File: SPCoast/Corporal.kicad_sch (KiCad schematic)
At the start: 36 parts, among them SW11829 829, SW11831 831, SW11900 829D, SW11901 1

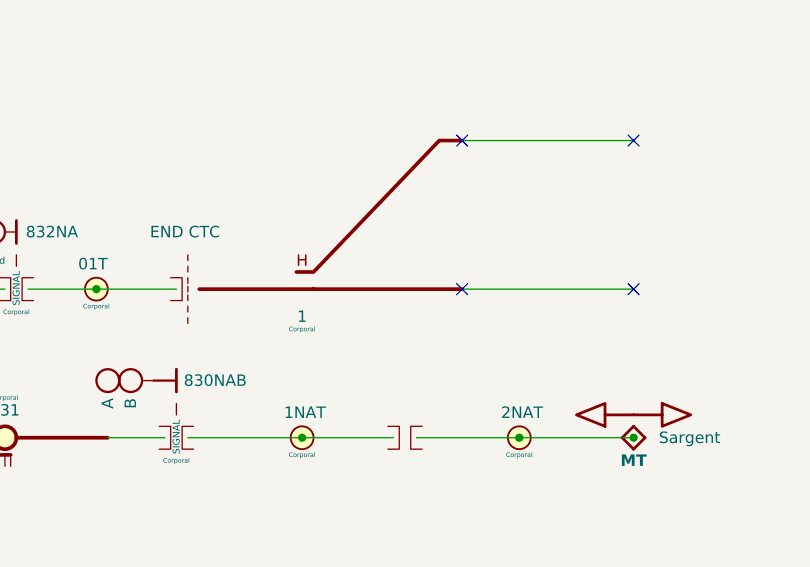
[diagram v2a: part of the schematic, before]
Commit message: feat(spcoast): every sheet on the four Railroad libraries (checkpoint step 6, mechanical half)
By SPCoast/edits/2026-10-12-migrate-libraries.py, run once with KiCad closed: 483 instances
remapped across 16 sheets, embedded definitions replaced by the library blocks, instance fields
synced (Kind, ControlToken, Vital, NormalIs, Chain, Index dropped; Indications renamed
IndicationCeiling; Hold_ms renamed hold_ms; a pixel's Index became its Address; Rulebook kept
on the four Luchessa markers because the compiler still reads it), and 22 units added at the
same position for the plates and devices that are multi-unit now. Owner's choices: every plant
head CPL; Sargent's semaphore UQ; the 0x27 PCA9685 as PWM; the office MAX7313s as the
SPCoastcTc variant. Left by hand: the two AUXILIARY_TRAFFIC markers on Watsonville (retired).

Verified (production/migration-gate.txt, netlist_diff.py against pre-migration.net): office
and local plates and all chips keep their connectivity; 14 nets lost, all on Sargent, where
the six field devices (DevSW13001, 13004 to 13007, 13012) have new pin positions and must be
re-wired by hand. ERC: lib_symbol_issues 492 before (unregistered libraries) to 2 after (the
retired markers); the 29 unconnected pins are those devices and their chip pins.

Co-Authored-By: Claude Fable 5.1 <noreply@anthropic.com>
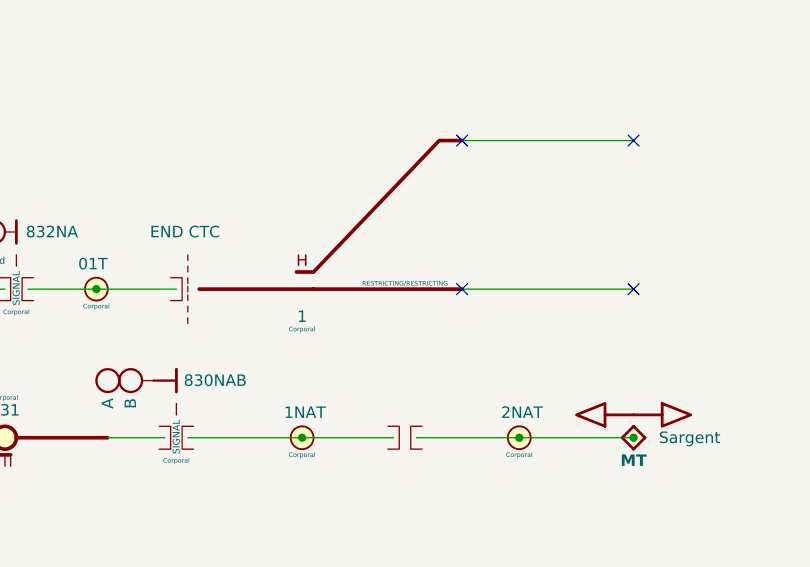
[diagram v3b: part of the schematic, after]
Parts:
- B11001, B11002, B11004, B11005: symbol Railroad:IRJ-Signal -> Railroad-Trackplan:IRJ-Signal
- B11003: symbol Railroad:IRJ-END_CTC -> Railroad-Trackplan:IRJ-END_CTC
- B11006, B11007: symbol Railroad:IRJ -> Railroad-Trackplan:IRJ
- CP11001, CP11002, CP11003: symbol Railroad:NextCP -> Railroad-Trackplan:NextCP
- DOT11002: symbol Railroad:Rule251-DoT-Left -> Railroad-Trackplan:Rule251-DoT-Left
- DOT11003: symbol Railroad:Rule251-DoT-Right -> Railroad-Trackplan:Rule251-DoT-Right
- DOT11004: symbol Railroad:Rule261-DoT-BiDirectional -> Railroad-Trackplan:Rule261-DoT-BiDirectional
- DOT11006: symbol Railroad:Rule105-RestrictedSpeed -> Railroad-Trackplan:Rule105-RestrictedSpeed
- H11001, H11002, H11003, H11004, H11005, H11006: symbol Railroad:Signal Head - CL -> Railroad-Trackplan:Signal Head - CPL; Appliance (none) -> head; Kind HEAD -> (none); Style (none) -> CPL
- HOUSE11001: symbol Railroad:MAIN HOUSE -> Railroad-Trackplan:MAIN HOUSE
- MC11001: symbol Railroad:MaintainerCall -> Railroad-Trackplan:MaintainerCall; Appliance (none) -> lamp; Kind MAINTAINER_CALL -> (none); Style (none) -> maintainer_call
- Plant11001: symbol Railroad:Interlocking -> Railroad-Trackplan:Interlocking
- S11001: symbol Railroad:Mast_Dwarf -> Railroad-Trackplan:Mast_Dwarf; Appliance (none) -> mast; Kind MAST_DWARF -> (none); Style (none) -> dwarf
- S11002, S11004: symbol Railroad:Mast_Double -> Railroad-Trackplan:Mast_Double; Appliance (none) -> mast; Kind MAST_DOUBLE -> (none); Style (none) -> double
- S11003: symbol Railroad:Mast_Single -> Railroad-Trackplan:Mast_Single; Appliance (none) -> mast; Kind MAST_SINGLE -> (none); Style (none) -> single
- SW11829: symbol Railroad:Switch_Lock -> Railroad-Trackplan:Switch_Lock; Appliance (none) -> switch; Kind SWITCH_LOCK -> (none); Style (none) -> lock
- SW11831: symbol Railroad:Switch_Powered -> Railroad-Trackplan:Switch_Powered; Appliance (none) -> switch; Kind SWITCH_REMOTE -> (none); Style (none) -> powered
- SW11900: symbol Railroad:Switch_Powered_Derail -> Railroad-Trackplan:Derail; Appliance (none) -> switch; IndicationCeiling (none) -> STOP/RESTRICTING; Indications STOP/RESTRICTING -> (none); Kind DERAIL -> (none); Style (none) -> derail
- SW11901: symbol Railroad:Switch_Manual_Sensed -> Railroad-Trackplan:Switch_Manual_Sensed; Appliance (none) -> switch; IndicationCeiling (none) -> RESTRICTING/RESTRICTING; Kind SWITCH_MANUAL -> (none); Style (none) -> manual_sensed
- TC11001, TC11002, TC11003, TC11004, TC11005: symbol Railroad:Track Circuit -> Railroad-Trackplan:Track Circuit; Appliance (none) -> track_circuit; Kind TRACK_CIRCUIT -> (none)

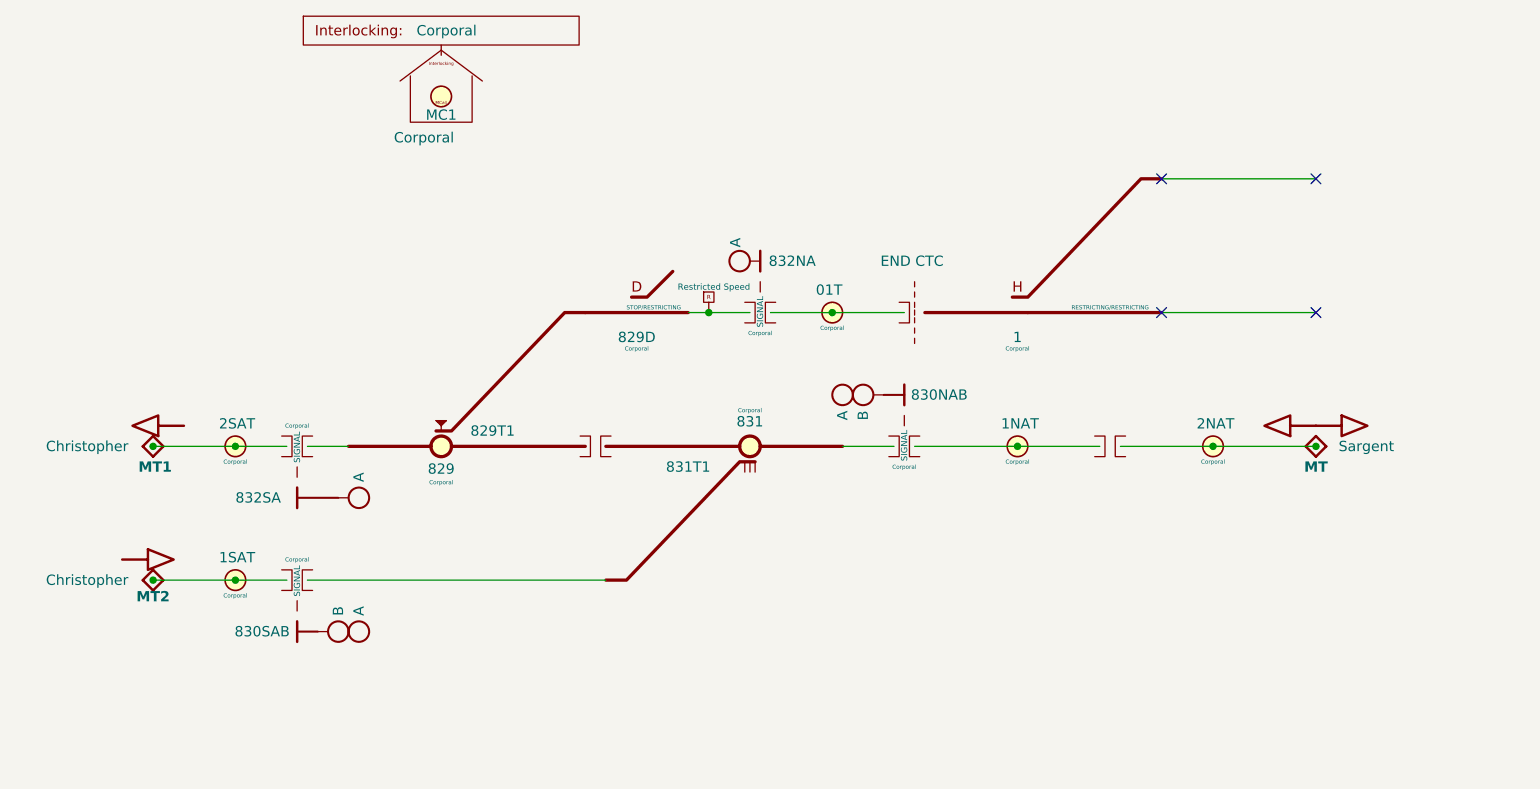
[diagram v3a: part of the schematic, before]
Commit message: chore: owner's Sargent cleanup and library edits of 2026-10-12 and 13 (baseline)
Co-Authored-By: Claude Fable 5.1 <noreply@anthropic.com>
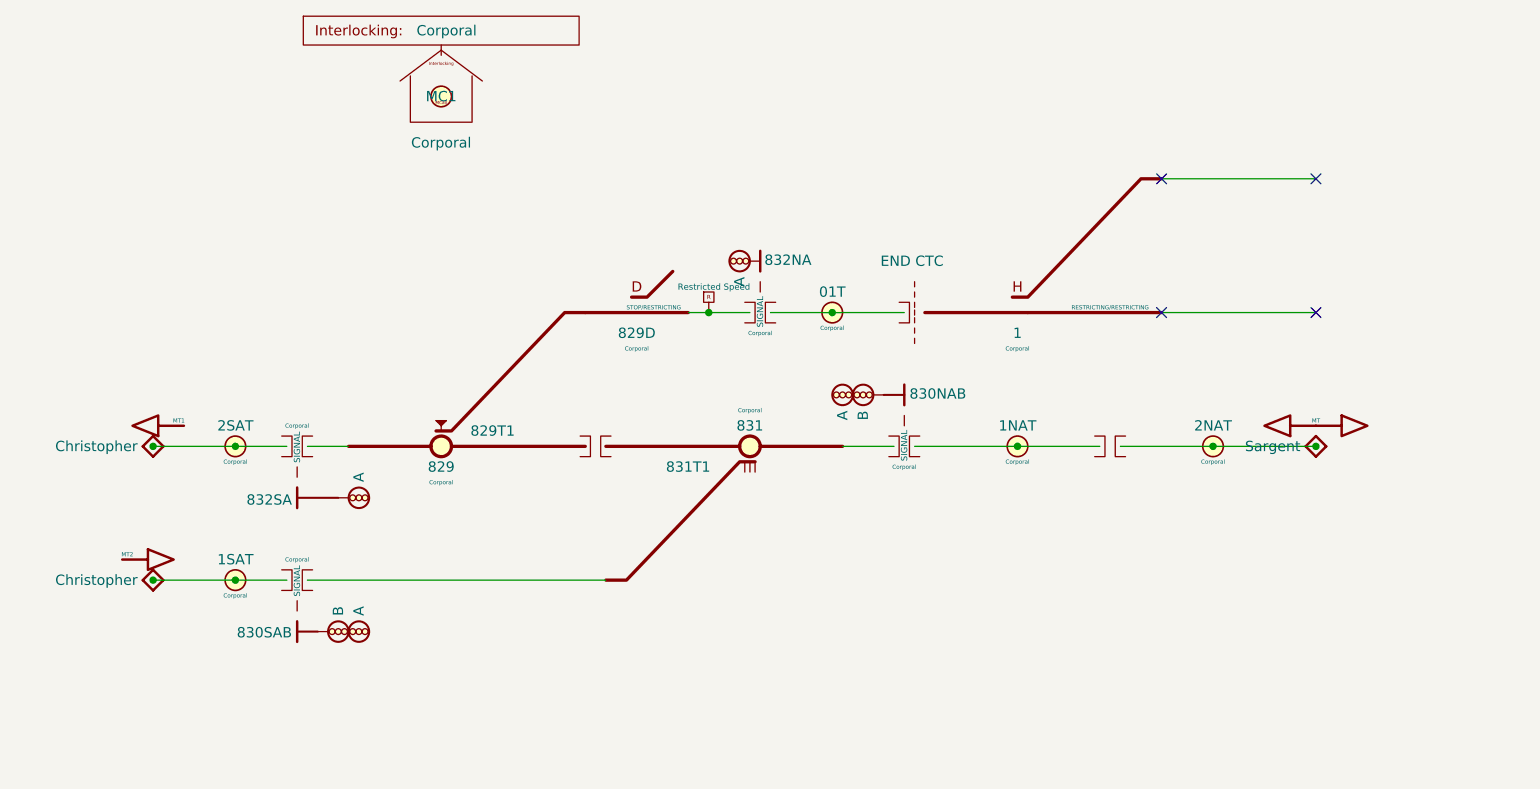
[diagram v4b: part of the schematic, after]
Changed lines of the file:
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@@
 		)
 		(property "Value" "Christopher"
-			(at 60.452 101.6 0)
+			(at 61.595 101.6 0)
 			(show_name no)
 			(do_not_autoplace no)
@@
 		)
 		(property "Value" "A"
-			(at 135.382 59.944 90)
+			(at 135.89 64.77 90)
 			(show_name no)
 			(do_not_autoplace yes)
@@
 		)
 		(property "Value" "829D"
-			(at 123.19 71.63 0)
+			(at 123.19 71.12 0)
 			(show_name no)
 			(do_not_autoplace no)
@@
 			(at 121.92 67.945 0)
 			(show_name no)
-			(do_not_autoplace no)
+			(do_not_autoplace yes)
 			(effects
 				(font
@@
 		)
 		(property "Value" "829"
-			(at 99.06 87.88 0)
+			(at 99.06 87.63 0)
 			(show_name no)
 			(do_not_autoplace no)
@@
 			(at 112.395 84.455 0)
 			(show_name no)
-			(do_not_autoplace no)
+			(do_not_autoplace yes)
 			(effects
 				(font
@@
 		)
 		(property "Appliance" "switch"
-			(at 99.06 85.09 0)
+			(at 92.075 78.74 0)
 			(hide yes)
 			(show_name no)
@@
 		)
 		(property "Style" "lock"
-			(at 99.06 85.09 0)
+			(at 92.075 78.74 0)
 			(hide yes)
 			(show_name no)
@@
 		)
 		(property "Value" "MT1"
-			(at 63.754 87.63 0)
+			(at 66.675 81.915 0)
 			(show_name no)
 			(do_not_autoplace yes)
 			(effects
 				(font
-					(size 1.27 1.27)
-					(thickness 0.254)
-					(bold yes)
+					(size 0.508 0.508)
 					(color 0 0 0 1)
 				)
@@
 		)
 		(property "Value" "830NAB"
-			(at 160.528 78.74 0)
+			(at 156.845 78.613 0)
 			(show_name no)
 			(do_not_autoplace yes)
@@
 					(size 1.27 1.27)
 				)
+				(justify left)
 			)
 		)
@@
 		)
 		(property "Value" "1"
-			(at 170.18 71.63 0)
+			(at 170.18 71.12 0)
 			(show_name no)
 			(do_not_autoplace no)
@@
 		)
 		(property "Appliance" "switch"
-			(at 170.18 68.58 0)
+			(at 168.275 73.025 0)
 			(hide yes)
 			(show_name no)
@@
 		)
 		(property "Style" "manual_sensed"
-			(at 170.18 68.58 0)
+			(at 168.275 73.025 0)
 			(hide yes)
 			(show_name no)
@@
 		)
 		(property "Value" "2NAT"
-			(at 192.28 82.3 0)
+			(at 194.31 82.55 0)
 			(show_name no)
 			(do_not_autoplace no)
@@
 					(size 1.27 1.27)
 				)
-				(justify left)
 			)
 		)
@@
 		)
 		(property "Value" "01T"
-			(at 145.29 65.79 0)
+			(at 147.32 66.04 0)
 			(show_name no)
 			(do_not_autoplace no)
@@
 					(size 1.27 1.27)
 				)
-				(justify left)
 			)
 		)
@@
 		)
 		(property "Value" "2SAT"
-			(at 71.63 82.3 0)
+			(at 73.66 82.55 0)
 			(show_name no)
 			(do_not_autoplace no)
@@
 					(size 1.27 1.27)
 				)
-				(justify left)
 			)
 		)
@@
 		)
 		(property "Value" "830SAB"
-			(at 76.962 107.95 0)
+			(at 80.645 108.077 0)
 			(show_name no)
 			(do_not_autoplace yes)
@@
 					(size 1.27 1.27)
 				)
+				(justify left)
 			)
 		)
@@
 		)
 		(property "Value" "Corporal"
-			(at 93.22 46.99 0)
+			(at 99.06 47.625 0)
 			(show_name no)
 			(do_not_autoplace no)
@@
 					(size 1.27 1.27)
 				)
-				(justify left)
 			)
 		)
@@
 		)
 		(property "Value" "832SA"
-			(at 73.66 91.44 0)
+			(at 80.645 91.694 0)
 			(show_name no)
 			(do_not_autoplace no)
@@
 					(size 1.27 1.27)
 				)
-				(justify right)
+				(justify left)
 			)
 		)
@@
 		)
 		(property "Value" "MT2"
-			(at 63.5 103.632 0)
+			(at 60.325 98.425 0)
 			(show_name no)
 			(do_not_autoplace yes)
 			(effects
 				(font
-					(size 1.27 1.27)
-					(thickness 0.254)
-					(bold yes)
+					(size 0.508 0.508)
 					(color 0 0 0 1)
 				)
@@
 		)
 		(property "Value" "831"
-			(at 137.16 82.04 0)
+			(at 137.16 82.55 0)
 			(show_name no)
 			(do_not_autoplace no)
@@
 			(at 123.825 85.725 0)
 			(show_name no)
-			(do_not_autoplace no)
+			(do_not_autoplace yes)
 			(effects
 				(font
@@
 		)
 		(property "Appliance" "switch"
-			(at 137.16 85.09 0)
+			(at 145.415 92.71 0)
 			(hide yes)
 			(show_name no)
@@
 		)
 		(property "Style" "powered"
-			(at 137.16 85.09 0)
+			(at 145.415 92.71 0)
 			(hide yes)
 			(show_name no)
@@
 		)
 		(property "Value" "Sargent"
-			(at 216.662 85.09 0)
+			(at 205.105 85.09 0)
 			(show_name no)
 			(do_not_autoplace no)
@@
 		)
 		(property "Value" "MC1"
-			(at 99.06 44.196 0)
+			(at 99.06 41.91 0)
 			(show_name no)
 			(do_not_autoplace no)
@@
 		)
 		(property "Value" "832NA"
-			(at 145.288 62.23 0)
+			(at 138.938 62.103 0)
 			(show_name no)
 			(do_not_autoplace yes)
@@
 					(size 1.27 1.27)
 				)
-				(justify right)
+				(justify left)
 			)
 		)
@@
 		)
 		(property "Value" "1NAT"
-			(at 168.15 82.3 0)
+			(at 170.18 82.55 0)
 			(show_name no)
 			(do_not_autoplace no)
@@
 					(size 1.27 1.27)
 				)
-				(justify left)
 			)
 		)
@@
 		)
 		(property "Value" "1SAT"
-			(at 71.63 98.81 0)
+			(at 73.66 99.06 0)
 			(show_name no)
 			(do_not_autoplace no)
@@
 					(size 1.27 1.27)
 				)
-				(justify left)
 			)
 		)
@@
 		)
 		(property "Value" "Christopher"
-			(at 60.452 85.09 0)
+			(at 61.595 85.09 0)
 			(show_name no)
 			(do_not_autoplace no)
@@
 		)
 		(property "Value" "MT"
-			(at 207.01 87.63 0)
+			(at 207.01 81.915 0)
 			(show_name no)
 			(do_not_autoplace yes)
 			(effects
 				(font
-					(size 1.27 1.27)
-					(thickness 0.254)
-					(bold yes)
+					(size 0.508 0.508)
 					(color 0 0 0 1)
 				)

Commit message: fix(spcoast): placed instances agree with their library symbols on Role, Appliance, Style
KiCad copies fields at placement and never follows the library. The 2026-10-12 migration
filled empty instance fields but kept non-empty ones, so heads placed before the libraries
were corrected still said Role COMPONENT and Style CPL. A compiler joining devices to
appliances by Appliance and Style (I9) would have failed on Sargent's CL and UQ heads.

The one-off `SPCoast/edits/2026-10-16-sync-library-fields.py` sets every library-owned
field (Role, Appliance, Style, IC, Kind, Pin.*) on every instance of a Railroad-* symbol
to the library's value, by text edit. 58 instances on 7 sheets: 53 heads to Role APPLIANCE
(Sargent's H1 to Style UQ and H2 to CL), two Mileposts to Role TRACK (ADR 0004 D7), the
Sargent Local plates to Role DEVICE (checkpoint E72), and 836SB's semaphore device to the
library's Style list `LQ, UQ`.

Front-end rule this records (owner, 2026-10-16): library-owned fields are read from the
library by lib_id, and an instance that disagrees is a diagnostic.

Verified:
- tools/contract/netlist_diff.py production/SPCoast.net production/post-sync.net: 493 nets,
  1086 nodes, 485 parts, connectivity identical
- kicad-cli sch erc --severity-all: 0 violations
- the script re-run reports 0 changes

Co-Authored-By: Claude Fable 5.1 <noreply@anthropic.com>
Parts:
- H11001, H11002, H11003, H11004, H11005, H11006: Role COMPONENT -> APPLIANCE
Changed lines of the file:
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@@
 			)
 		)
-		(property "Role" "COMPONENT"
+		(property "Role" "APPLIANCE"
 			(at 139.7 64.77 0)
 			(hide yes)
@@
 			)
 		)
-		(property "Role" "COMPONENT"
+		(property "Role" "APPLIANCE"
 			(at 154.94 81.28 0)
 			(hide yes)
@@
 			)
 		)
-		(property "Role" "COMPONENT"
+		(property "Role" "APPLIANCE"
 			(at 152.4 81.28 0)
 			(hide yes)
@@
 			)
 		)
-		(property "Role" "COMPONENT"
+		(property "Role" "APPLIANCE"
 			(at 82.55 105.41 0)
 			(hide yes)
@@
 			)
 		)
-		(property "Role" "COMPONENT"
+		(property "Role" "APPLIANCE"
 			(at 85.09 88.9 0)
 			(hide yes)
@@
 			)
 		)
-		(property "Role" "COMPONENT"
+		(property "Role" "APPLIANCE"
 			(at 85.09 105.41 0)
 			(hide yes)
